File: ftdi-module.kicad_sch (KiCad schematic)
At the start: 51 parts, among them J1 USB3106-30-0230-A, U1 FT2232HL-REEL, U2 ISO1641, U3 NCP163ASN330T1G, Y1 KX-7_12,MHz

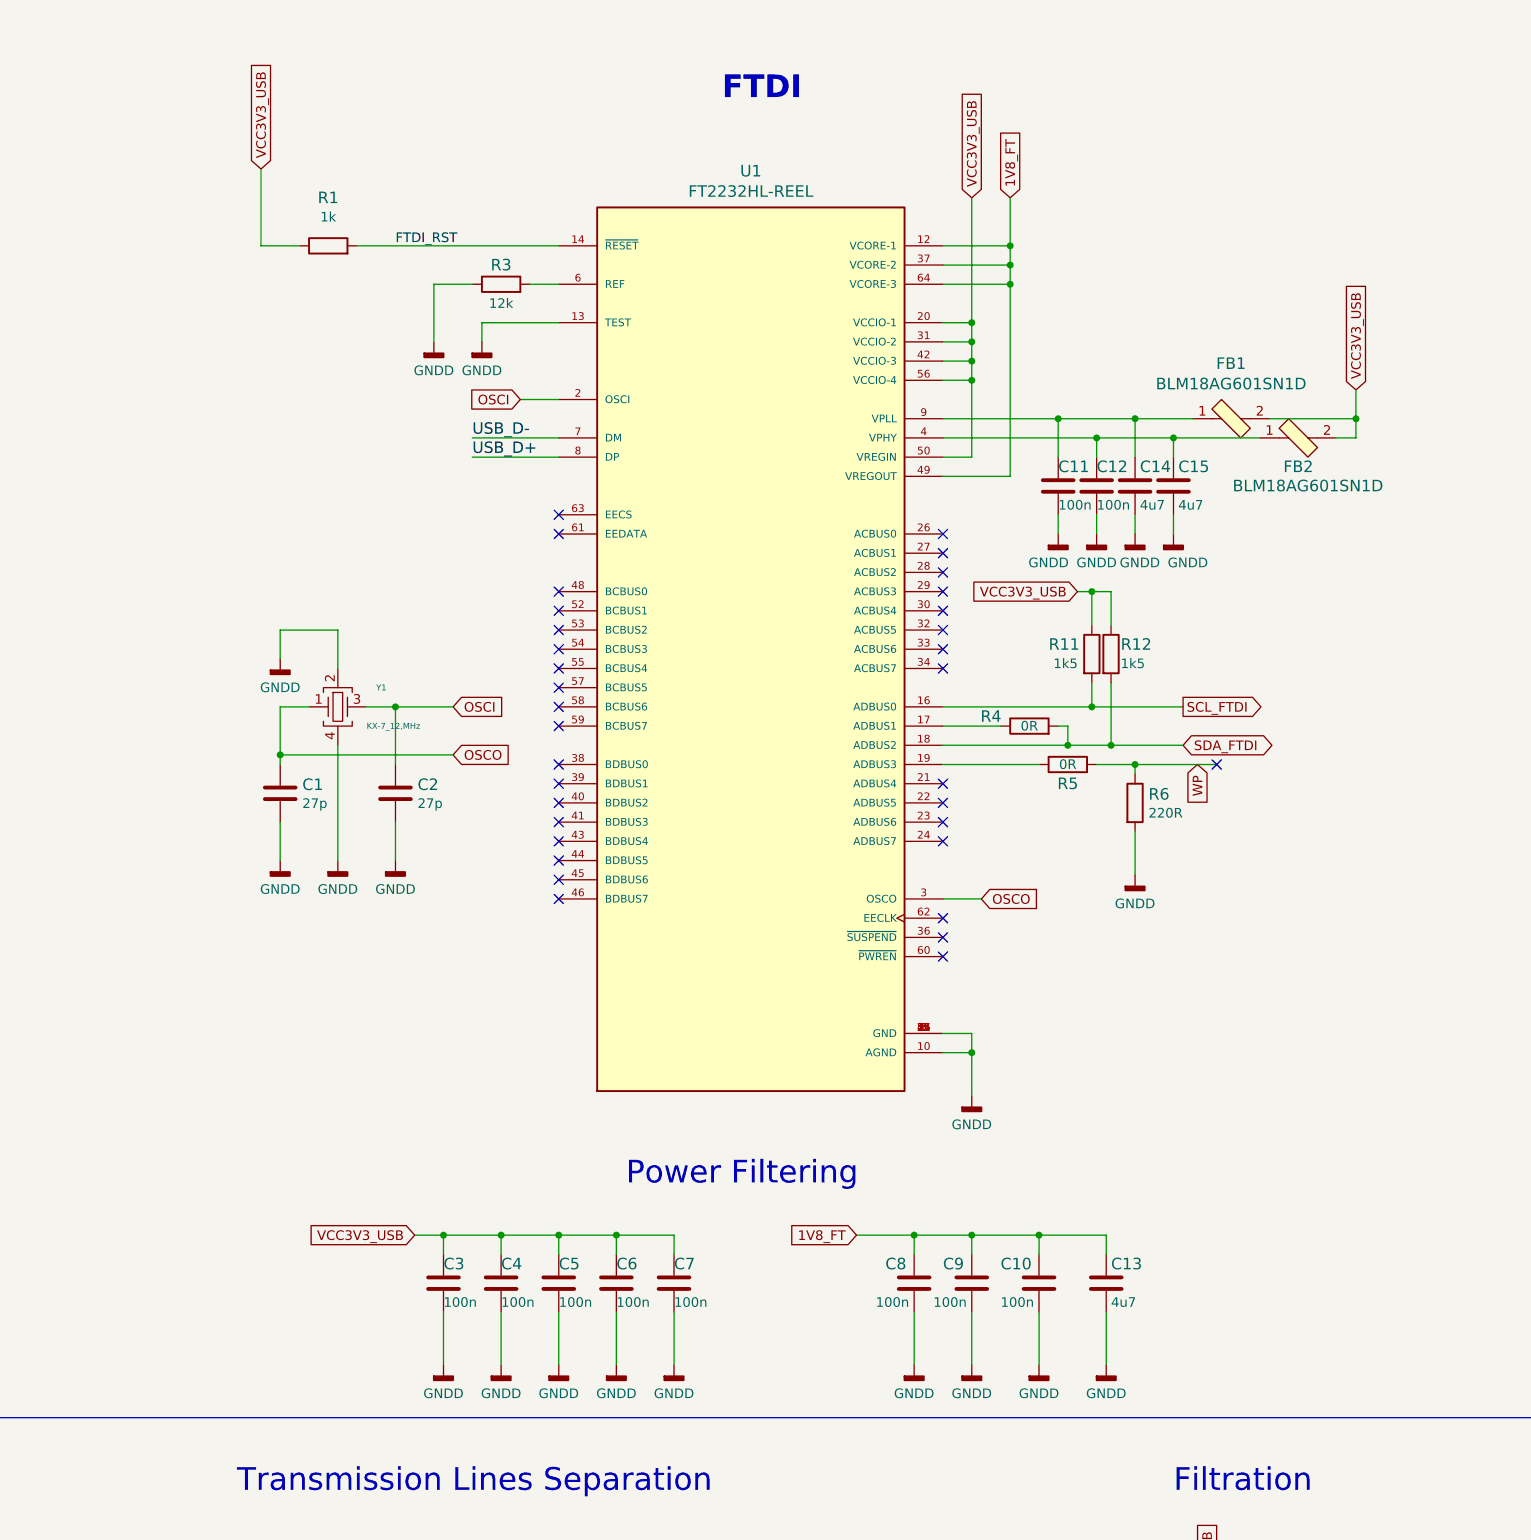
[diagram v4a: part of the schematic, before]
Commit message: Replaced FTDI chip with FT4232H-56Q on the schematic
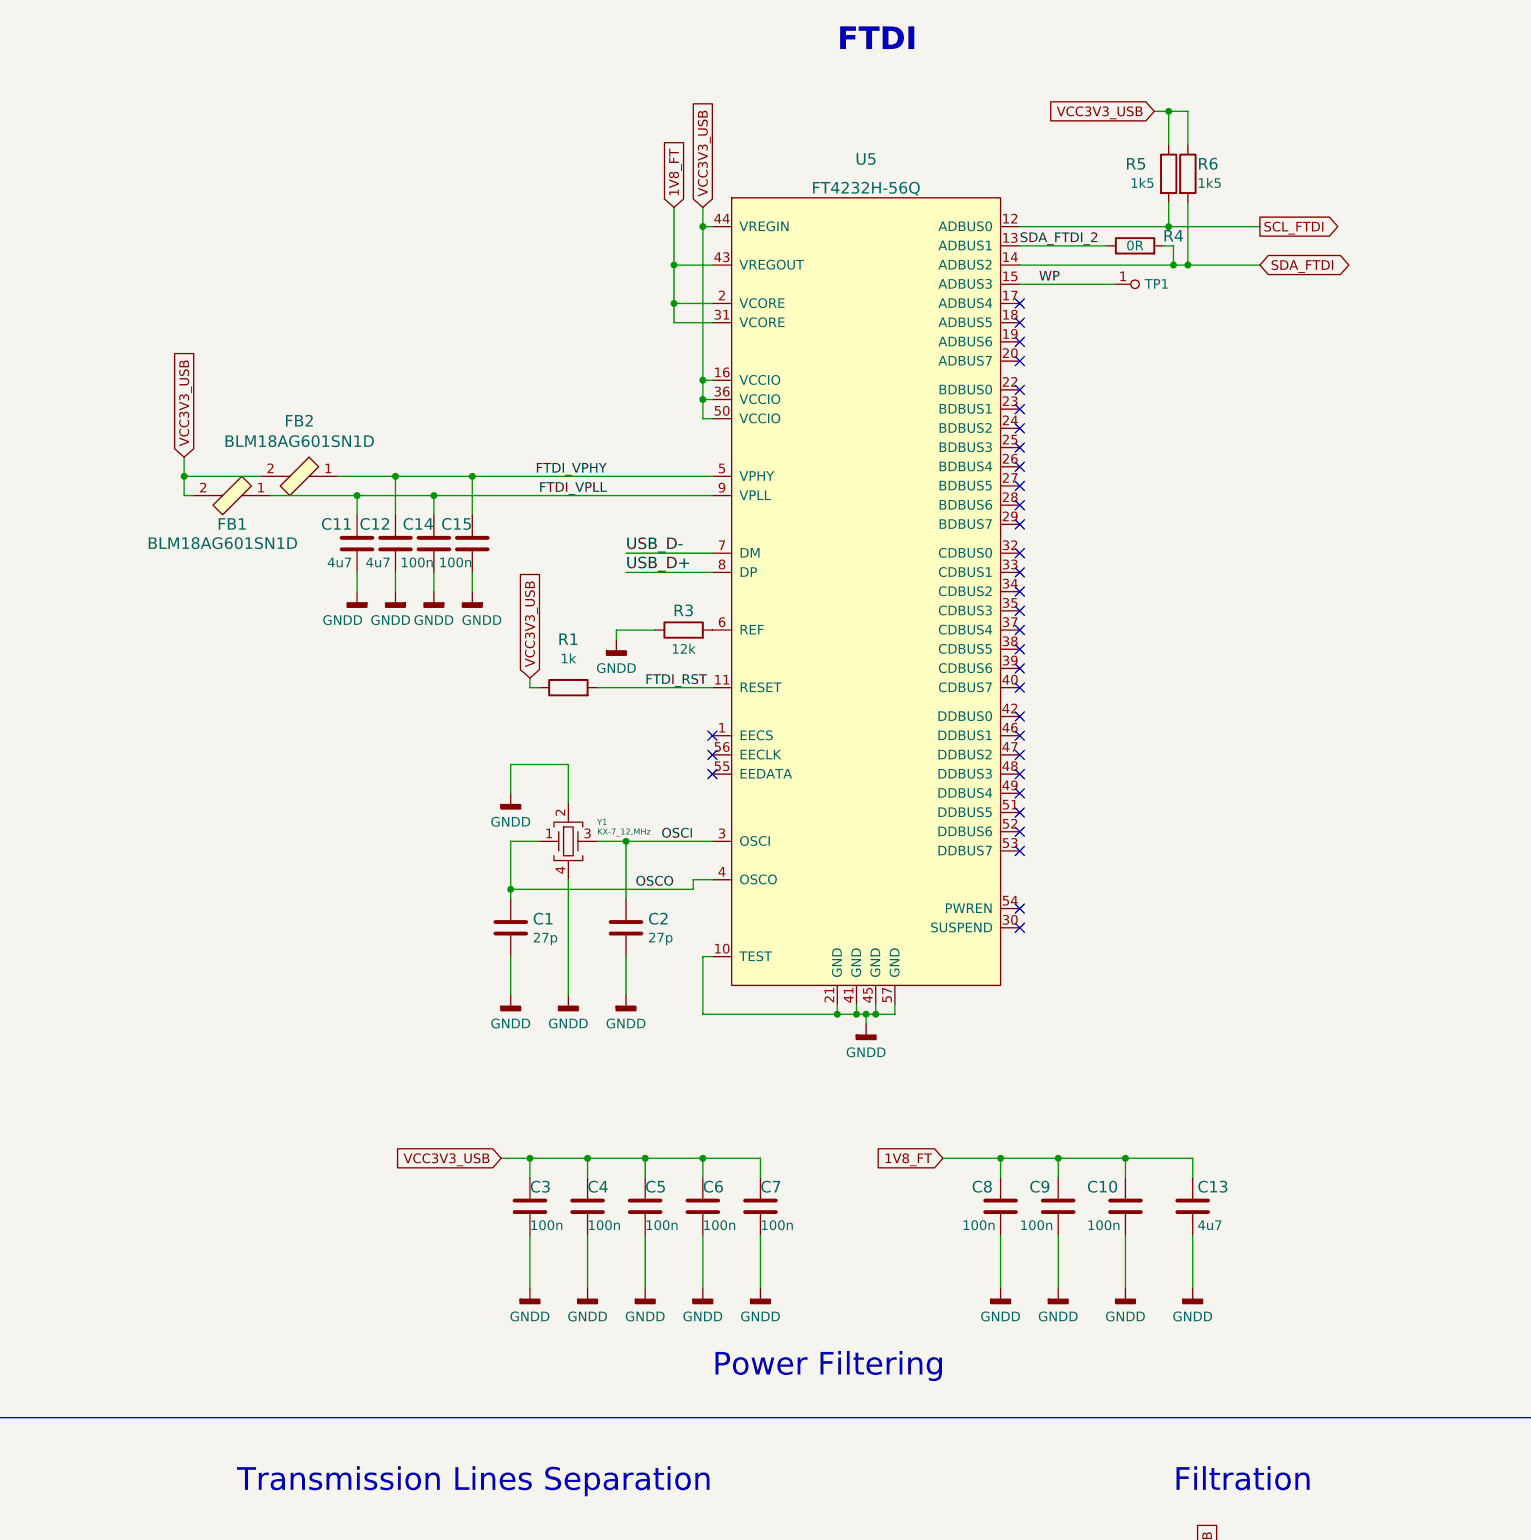
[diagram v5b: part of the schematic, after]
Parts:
- removed C11, C12: C_100n_0402, nuc-compute-cluster-power-breakout-footprints:0402-cap, symbol nuc-compute-cluster-power-breakout:C_100n_0402
- removed C14, C15: C_4u7_0402, nuc-compute-cluster-power-breakout-footprints:0402-cap, symbol nuc-compute-cluster-power-breakout:C_4u7_0402
- removed R11, R12: R_1k5_0402, nuc-compute-cluster-power-breakout-footprints:0402-res, symbol nuc-compute-cluster-power-breakout:R_1k5_0402
- removed R5: R_0R_0603, nuc-compute-cluster-power-breakout-footprints:0603-res, symbol nuc-compute-cluster-power-breakout:R_0R_0603
- removed R6: R_220R_0402, nuc-compute-cluster-power-breakout-footprints:0402-res, symbol nuc-compute-cluster-power-breakout:R_220R_0402
- removed U1: FT2232HL-REEL, nuc-compute-cluster-power-breakout-footprints:LQFP-64_10x10mm, symbol nuc-compute-cluster-power-breakout:FT2232HL-REEL
- added C11, C12: C_4u7_0402, nuc-compute-cluster-power-breakout-footprints:0402-cap, symbol nuc-compute-cluster-power-breakout:C_4u7_0402
- added C14, C15: C_100n_0402, nuc-compute-cluster-power-breakout-footprints:0402-cap, symbol nuc-compute-cluster-power-breakout:C_100n_0402
- added R5, R6: R_1k5_0402, nuc-compute-cluster-power-breakout-footprints:0402-res, symbol nuc-compute-cluster-power-breakout:R_1k5_0402
- added TP1: TP, antmicro-footprints:TP-R-1.5, symbol antmicroTestPoints:TP
- added U5: FT4232H-56Q, antmicro-footprints:QFN-56-1EP_8x8mm_P0.5mm_EP5.5.9x5.9mm, symbol antmicroInterfaceControllers:FT4232H-56Q
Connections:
- net 1V8_FT: now also U5.2 (VCORE), U5.31 (VCORE), U5.43 (VREGOUT)
- net FTDI_RST: now also U5.11 (RESET)
- net GNDD: now also C11.2, C12.2, C14.2, C15.2, U5.10 (TEST), U5.21 (GND), U5.41 (GND), U5.45 (GND), U5.57 (GND)
- net OSCI: now also U5.3 (OSCI)
- net OSCO: now also U5.4 (OSCO)
- net SCL_FTDI: now also R5.2, U5.12 (ADBUS0)
- net SDA_FTDI: now also R6.2, U5.14 (ADBUS2)
- net USB_D+: now also U5.8 (DP)
- net USB_D-: now also U5.7 (DM)
- net VCC3V3_USB: now also R5.1, R6.1, U5.16 (VCCIO), U5.36 (VCCIO), U5.44 (VREGIN), U5.50 (VCCIO)
- net WP: now also TP1.1, U5.15 (ADBUS3)
- net SDA_FTDI_2: now reaches R4.1
- net SDA_FTDI_2: now also U5.13 (ADBUS1)
- net FTDI_VPHY: now reaches FB2.1
- net FTDI_VPHY: now also C12.1, C15.1, U5.5 (VPHY)
- net at R3.2: now also U5.6 (REF)
- net FTDI_VPLL: now reaches FB1.1
- net FTDI_VPLL: now also C11.1, C14.1, U5.9 (VPLL)
- no-connect marks 35 -> 34
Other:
- moved on the sheet: C1, C10, C13, C2, C3, C4, C5, C6, C7, C8, C9, Y1
